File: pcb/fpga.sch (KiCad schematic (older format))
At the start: 17 parts, among them J1 CONN_INTEGRALSTICK_FPGA_DEVICE, Q1 SSM6N58NU, U12 DSC6001HI2A-025.0000‎, U2 XC7A50T-1FTG256C, U9 AT24MAC402-UDFN

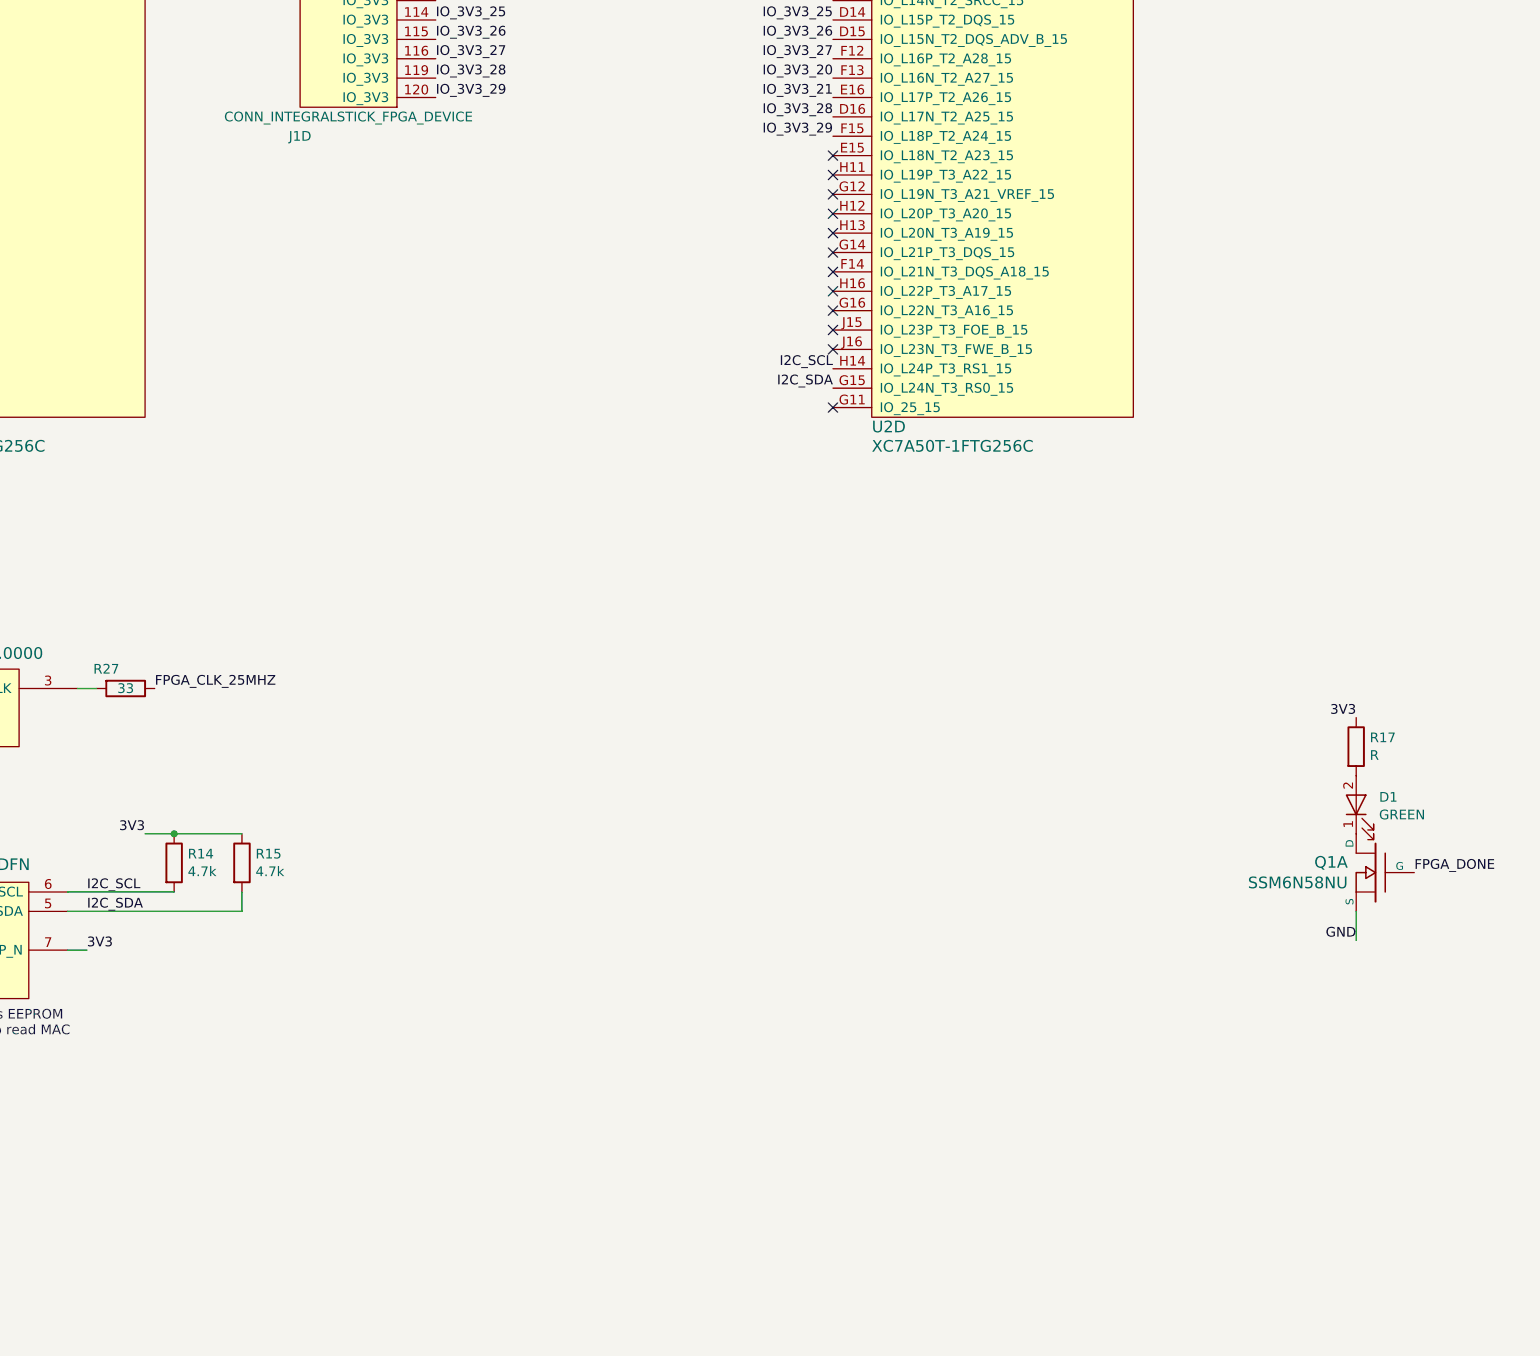
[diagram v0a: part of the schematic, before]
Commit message: Added four GPIO LEDs
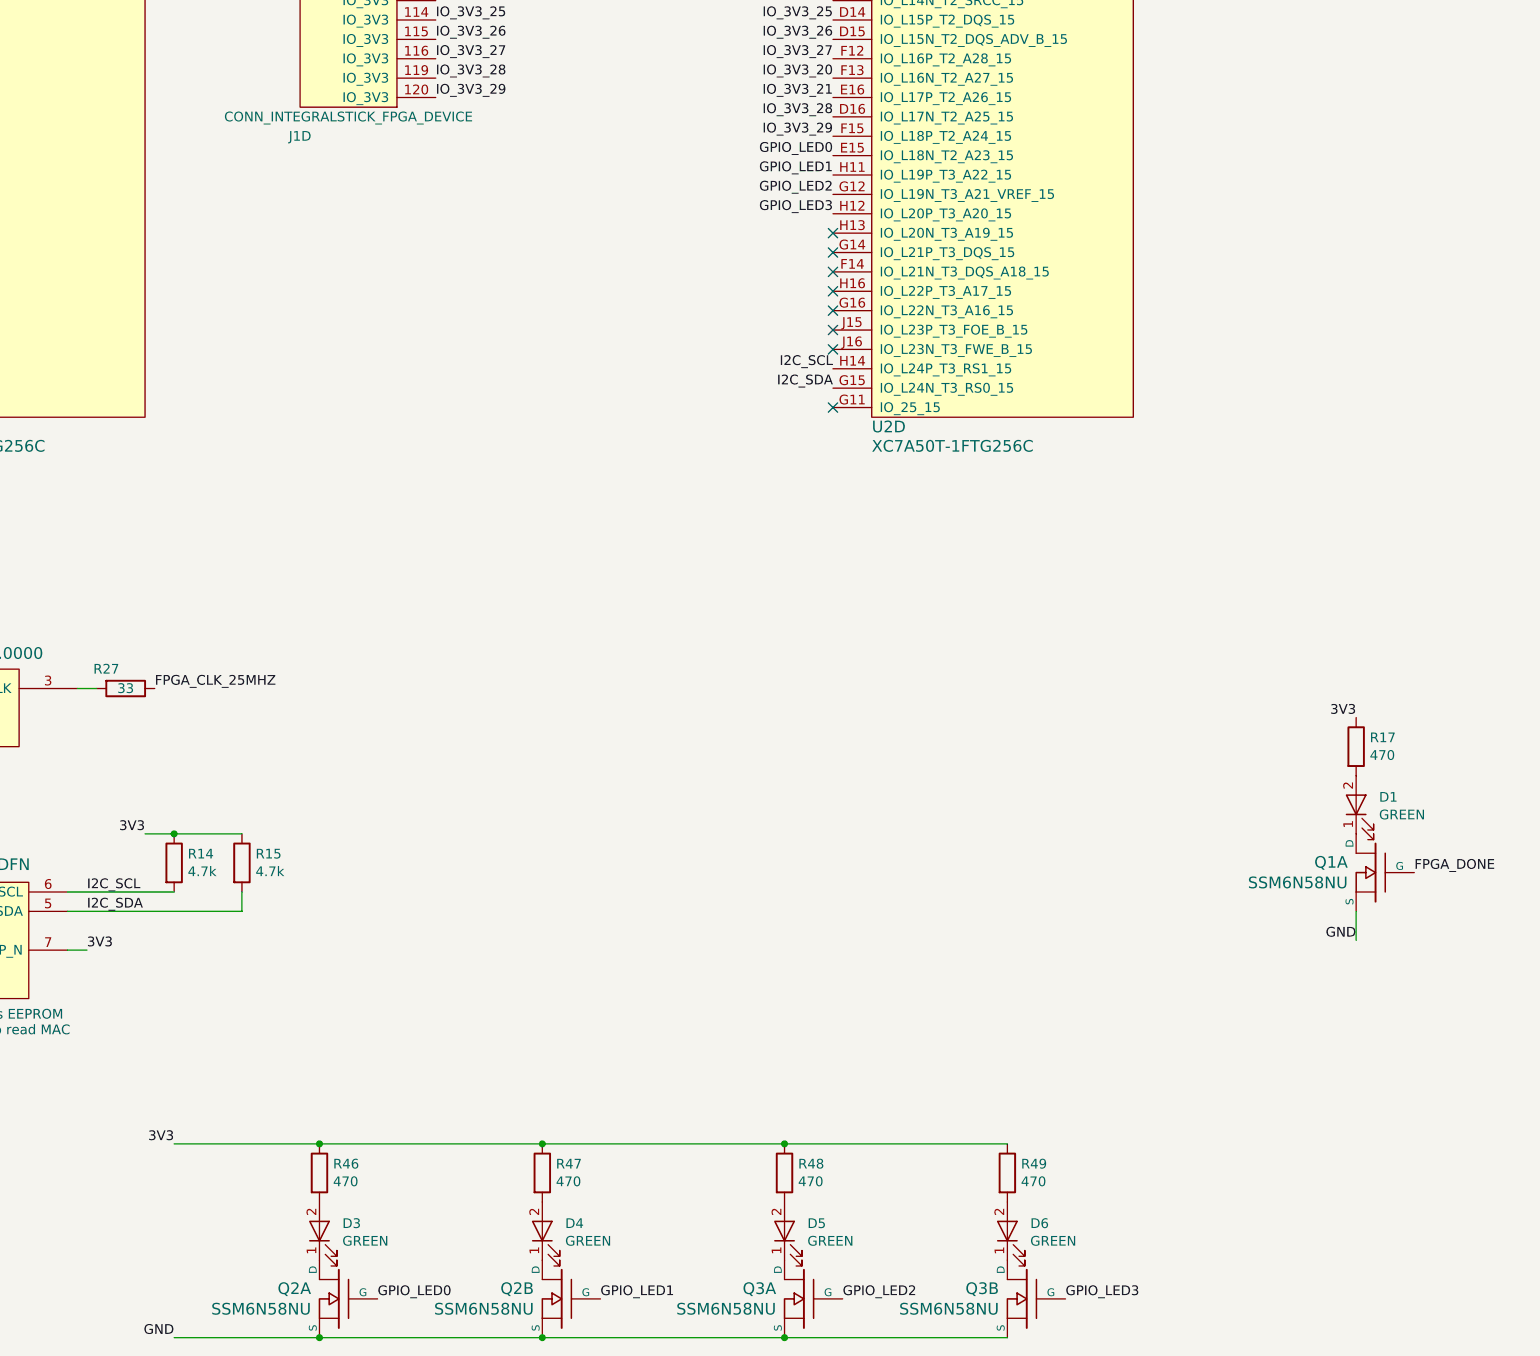
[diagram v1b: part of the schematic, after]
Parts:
- added D3, D4, D5, D6: GREEN, symbol device:LED
- added Q2, Q3: SSM6N58NU, symbol special-azonenberg:SSM6N58NU_DUAL_NMOS
- added R46, R47, R48, R49: 470, symbol device:R
- R17: value R -> 470
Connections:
- net 3V3: now also R46.1, R47.1, R48.1, R49.1
- net GND: now also Q2.S1 (S), Q2.S2 (S), Q3.S1 (S), Q3.S2 (S)
- net GPIO_LED0: now reaches U2.E15 (IO_L18N_T2_A23_15)
- net GPIO_LED0: now also Q2.G1 (G)
- net GPIO_LED2: now reaches U2.G12 (IO_L19N_T3_A21_VREF_15)
- net GPIO_LED2: now also Q3.G1 (G)
- net GPIO_LED1: now reaches U2.H11 (IO_L19P_T3_A22_15)
- net GPIO_LED1: now also Q2.G2 (G)
- net GPIO_LED3: now reaches U2.H12 (IO_L20P_T3_A20_15)
- net GPIO_LED3: now also Q3.G2 (G)
- new net: D3.1 (K), Q2.D1 (D)
- new net: D3.2 (A), R46.2
- new net: D4.1 (K), Q2.D2 (D)
- new net: D4.2 (A), R47.2
- new net: D5.1 (K), Q3.D1 (D)
- new net: D5.2 (A), R48.2
- new net: D6.1 (K), Q3.D2 (D)
- new net: D6.2 (A), R49.2
- no-connect marks 14 -> 10
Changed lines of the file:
@@
 Text Label 8400 3150 2    50   ~ 0
 IN_3V3_0_N
-NoConn ~ 8400 4350
-NoConn ~ 8400 4450
-NoConn ~ 8400 4550
-NoConn ~ 8400 4650
 NoConn ~ 8400 4750
 NoConn ~ 8400 4850
@@
 P 11100 7400
 F 0 "R17" H 11170 7446 50  0000 L CNN
-F 1 "R" H 11170 7355 50  0000 L CNN
+F 1 "470" H 11170 7355 50  0000 L CNN
 F 2 "" V 11030 7400 50  0001 C CNN
 F 3 "" H 11100 7400 50  0001 C CNN
@@
 Text HLabel 2650 8250 0    50   Input ~ 0
 GND
+$Comp
+L special-azonenberg:SSM6N58NU_DUAL_NMOS Q2
+U 1 1 5D2CD0DE
+P 5850 10250
+F 0 "Q2" H 5993 10303 60  0000 L CNN
+F 1 "SSM6N58NU" H 5993 10197 60  0000 L CNN
+F 2 "" H 5850 10250 60  0000 C CNN
+F 3 "" H 5993 10144 60  0000 L CNN
+	1    5850 10250
+	-1   0    0    -1
+$EndComp
+$Comp
+L device:R R46
+U 1 1 5D2CDD46
+P 5750 9600
+F 0 "R46" H 5820 9646 50  0000 L CNN
+F 1 "470" H 5820 9555 50  0000 L CNN
+F 2 "" V 5680 9600 50  0001 C CNN
+F 3 "" H 5750 9600 50  0001 C CNN
+	1    5750 9600
+	1    0    0    -1
+$EndComp
+$Comp
+L device:LED D3
+U 1 1 5D2CEDB6
+P 5750 9900
+F 0 "D3" V 5789 9782 50  0000 R CNN
+F 1 "GREEN" V 5698 9782 50  0000 R CNN
+F 2 "" H 5750 9900 50  0001 C CNN
+F 3 "" H 5750 9900 50  0001 C CNN
+	1    5750 9900
+	0    -1   -1   0
+$EndComp
+Text Label 6050 10250 0    50   ~ 0
+GPIO_LED0
+$Comp
+L special-azonenberg:SSM6N58NU_DUAL_NMOS Q2
+U 2 1 5D2CF813
+P 7000 10250
+F 0 "Q2" H 7143 10303 60  0000 L CNN
+F 1 "SSM6N58NU" H 7143 10197 60  0000 L CNN
+F 2 "" H 7000 10250 60  0000 C CNN
+F 3 "" H 7143 10144 60  0000 L CNN
+	2    7000 10250
+	-1   0    0    -1
+$EndComp
+$Comp
+L device:R R47
+U 1 1 5D2CF81D
+P 6900 9600
+F 0 "R47" H 6970 9646 50  0000 L CNN
+F 1 "470" H 6970 9555 50  0000 L CNN
+F 2 "" V 6830 9600 50  0001 C CNN
+F 3 "" H 6900 9600 50  0001 C CNN
+	1    6900 9600
+	1    0    0    -1
+$EndComp
+$Comp
+L device:LED D4
+U 1 1 5D2CF827
+P 6900 9900
+F 0 "D4" V 6939 9782 50  0000 R CNN
+F 1 "GREEN" V 6848 9782 50  0000 R CNN
+F 2 "" H 6900 9900 50  0001 C CNN
+F 3 "" H 6900 9900 50  0001 C CNN
+	1    6900 9900
+	0    -1   -1   0
+$EndComp
+Text Label 7200 10250 0    50   ~ 0
+GPIO_LED1
+$Comp
+L special-azonenberg:SSM6N58NU_DUAL_NMOS Q3
+U 1 1 5D2D4ED9
+P 8250 10250
+F 0 "Q3" H 8393 10303 60  0000 L CNN
+F 1 "SSM6N58NU" H 8393 10197 60  0000 L CNN
+F 2 "" H 8250 10250 60  0000 C CNN
+F 3 "" H 8393 10144 60  0000 L CNN
+	1    8250 10250
+	-1   0    0    -1
+$EndComp
+$Comp
+L device:R R48
+U 1 1 5D2D4EE3
+P 8150 9600
+F 0 "R48" H 8220 9646 50  0000 L CNN
+F 1 "470" H 8220 9555 50  0000 L CNN
+F 2 "" V 8080 9600 50  0001 C CNN
+F 3 "" H 8150 9600 50  0001 C CNN
+	1    8150 9600
+	1    0    0    -1
+$EndComp
+$Comp
+L device:LED D5
+U 1 1 5D2D4EED
+P 8150 9900
+F 0 "D5" V 8189 9782 50  0000 R CNN
+F 1 "GREEN" V 8098 9782 50  0000 R CNN
+F 2 "" H 8150 9900 50  0001 C CNN
+F 3 "" H 8150 9900 50  0001 C CNN
+	1    8150 9900
+	0    -1   -1   0
+$EndComp
+Text Label 8450 10250 0    50   ~ 0
+GPIO_LED2
+$Comp
+L special-azonenberg:SSM6N58NU_DUAL_NMOS Q3
+U 2 1 5D2D4EF8
+P 9400 10250
+F 0 "Q3" H 9543 10303 60  0000 L CNN
+F 1 "SSM6N58NU" H 9543 10197 60  0000 L CNN
+F 2 "" H 9400 10250 60  0000 C CNN
+F 3 "" H 9543 10144 60  0000 L CNN
+	2    9400 10250
+	-1   0    0    -1
+$EndComp
+$Comp
+L device:R R49
+U 1 1 5D2D4F02
+P 9300 9600
+F 0 "R49" H 9370 9646 50  0000 L CNN
+F 1 "470" H 9370 9555 50  0000 L CNN
+F 2 "" V 9230 9600 50  0001 C CNN
+F 3 "" H 9300 9600 50  0001 C CNN
+	1    9300 9600
+	1    0    0    -1
+$EndComp
+$Comp
+L device:LED D6
+U 1 1 5D2D4F0C
+P 9300 9900
+F 0 "D6" V 9339 9782 50  0000 R CNN
+F 1 "GREEN" V 9248 9782 50  0000 R CNN
+F 2 "" H 9300 9900 50  0001 C CNN
+F 3 "" H 9300 9900 50  0001 C CNN
+	1    9300 9900
+	0    -1   -1   0
+$EndComp
+Text Label 9600 10250 0    50   ~ 0
+GPIO_LED3
+Text Label 5000 10450 2    50   ~ 0
+GND
+Wire Wire Line
+	5000 10450 5750 10450
+Connection ~ 5750 10450
+Wire Wire Line
+	5750 10450 6900 10450
+Connection ~ 6900 10450
+Wire Wire Line
+	6900 10450 8150 10450
+Connection ~ 8150 10450
+Wire Wire Line
+	8150 10450 9300 10450
+Text Label 5000 9450 2    50   ~ 0
+3V3
+Wire Wire Line
+	5000 9450 5750 9450
+Connection ~ 5750 9450
+Wire Wire Line
+	5750 9450 6900 9450
+Connection ~ 6900 9450
+Wire Wire Line
+	6900 9450 8150 9450
+Connection ~ 8150 9450
+Wire Wire Line
+	8150 9450 9300 9450
+Text Label 8400 4350 2    50   ~ 0
+GPIO_LED0
+Text Label 8400 4450 2    50   ~ 0
+GPIO_LED1
+Text Label 8400 4550 2    50   ~ 0
+GPIO_LED2
+Text Label 8400 4650 2    50   ~ 0
+GPIO_LED3
 $EndSCHEMATC

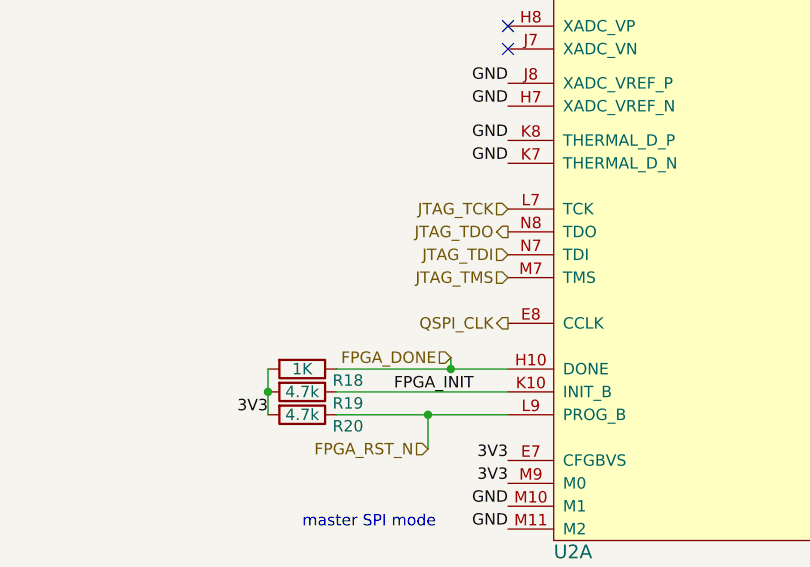
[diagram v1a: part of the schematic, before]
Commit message: Finished schematic signoff review. Fixed oscillator pinout bug, added some test points.
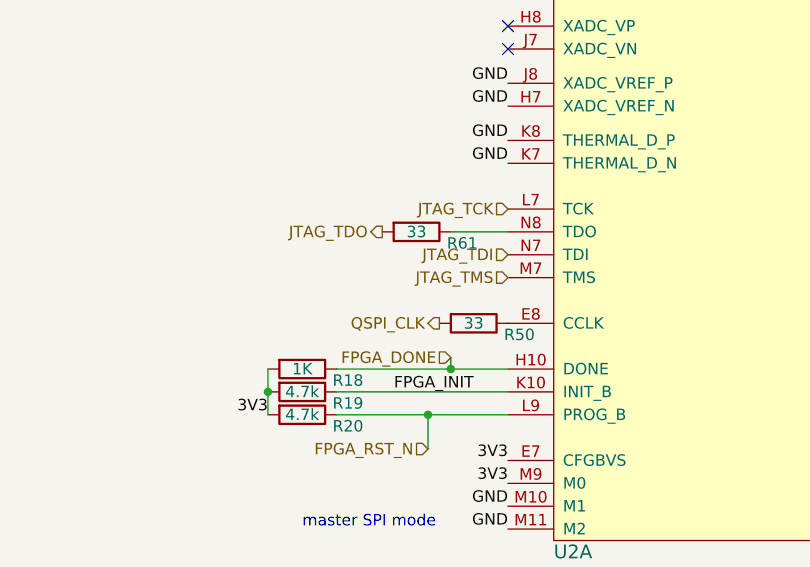
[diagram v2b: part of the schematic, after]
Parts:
- added R50, R61: 33, symbol device:R
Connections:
- net JTAG_TDO: now also R61.2; no longer U2.N8 (TDO)
- net QSPI_CLK: now also R50.2; no longer U2.E8 (CCLK)
- new net: R50.1, U2.E8 (CCLK)
- new net: R61.1, U2.N8 (TDO)
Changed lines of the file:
@@
 Sheet 6 8
 Title "INTEGRALSTICK Compute Module"
-Date "2018-11-07"
+Date "2018-11-09"
 Rev "0.1"
 Comp "Andrew D. Zonenberg"
@@
 Text HLabel 13900 4250 0    50   Input ~ 0
 JTAG_TCK
-Text HLabel 13900 4350 0    50   Output ~ 0
+Text HLabel 13350 4350 0    50   Output ~ 0
 JTAG_TDO
 Text HLabel 13900 4450 0    50   Input ~ 0
@@
 Text HLabel 13900 4550 0    50   Input ~ 0
 JTAG_TMS
-Text HLabel 13900 4750 0    50   Output ~ 0
+Text HLabel 13600 4750 0    50   Output ~ 0
 QSPI_CLK
 Text Label 13900 5350 2    50   ~ 0
@@
 Text Label 8400 4650 2    50   ~ 0
 GPIO_LED3
+$Comp
+L device:R R50
+U 1 1 5D36315D
+P 13750 4750
+F 0 "R50" V 13800 4950 50  0000 C CNN
+F 1 "33" V 13750 4750 50  0000 C CNN
+F 2 "" V 13680 4750 50  0001 C CNN
+F 3 "" H 13750 4750 50  0001 C CNN
+	1    13750 4750
+	0    1    1    0
+$EndComp
+$Comp
+L device:R R61
+U 1 1 5D3F599B
+P 13500 4350
+F 0 "R61" V 13550 4550 50  0000 C CNN
+F 1 "33" V 13500 4350 50  0000 C CNN
+F 2 "" V 13430 4350 50  0001 C CNN
+F 3 "" H 13500 4350 50  0001 C CNN
+	1    13500 4350
+	0    1    1    0
+$EndComp
+Wire Wire Line
+	13650 4350 13900 4350
 $EndSCHEMATC
